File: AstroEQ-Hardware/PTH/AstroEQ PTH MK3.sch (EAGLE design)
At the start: 46 parts, among them IC1 ATMEGA162-16PU, IC2 PIC18F14K50-I/P, IC3 78L05, J1 POWER_JACKPTH, M1 Motor Driver, M2 Motor Driver, X1 16MHz, X2 12MHz

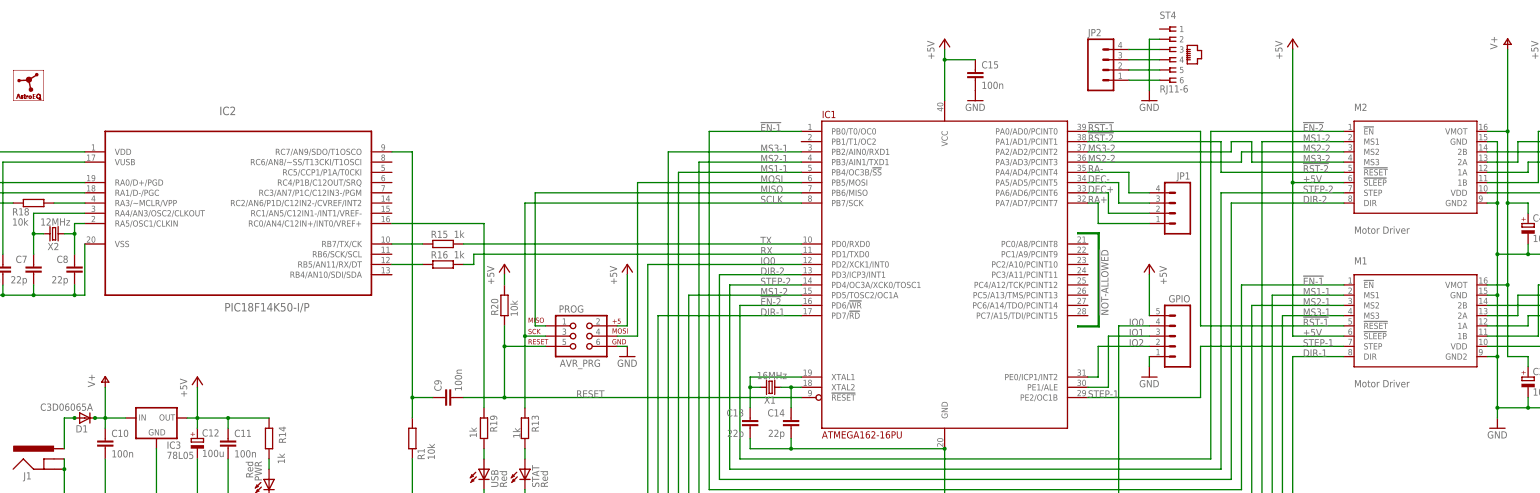
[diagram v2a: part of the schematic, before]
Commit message: Correct Schematic Labelling
Correct labelling in schematic and add additional information to avoid confusion with pin assignments on driver boards.
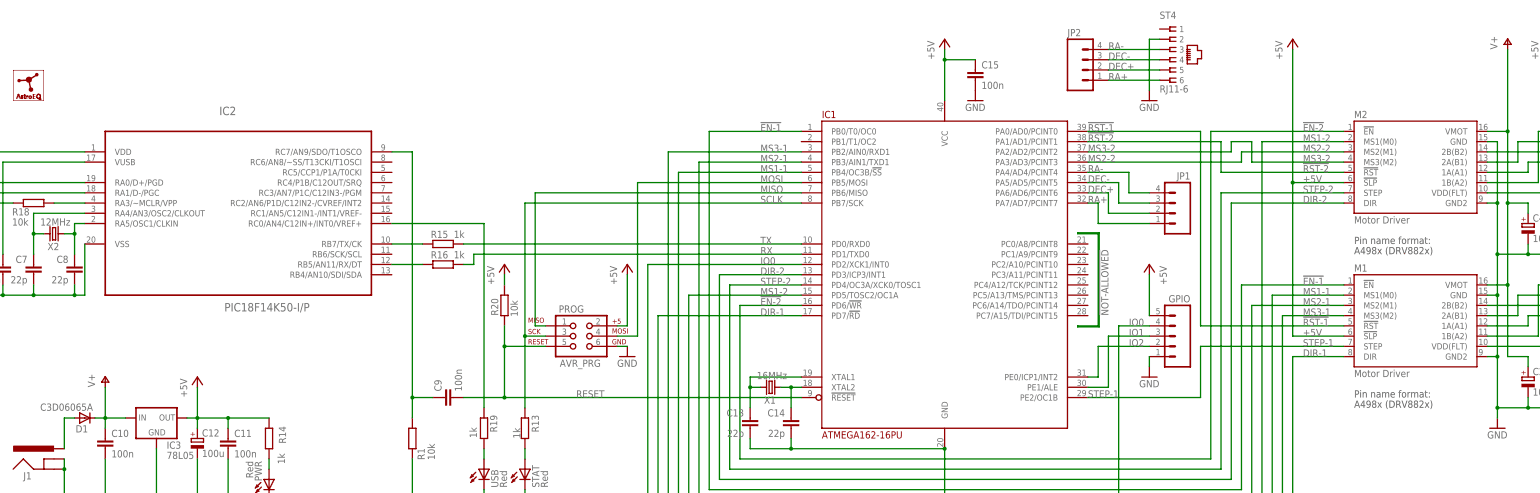
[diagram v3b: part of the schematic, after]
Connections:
- net !RST-1: now also M1.!RST; no longer M1.!RESET
- net !RST-2: now also M2.!RST; no longer M2.!RESET
- net +5V: now also M1.!SLP, M1.VDD(FLT), M2.!SLP, M2.VDD(FLT); no longer M1.!SLEEP, M1.VDD, M2.!SLEEP, M2.VDD
- net DEC-1A: now also M1.1A(A1); no longer M1.1A
- net DEC-1B: now also M1.1B(A2); no longer M1.1B
- net DEC-2A: now also M1.2A(B1); no longer M1.2A
- net DEC-2B: now also M1.2B(B2); no longer M1.2B
- net MS1-1: now also M1.MS1(M0); no longer M1.MS1
- net MS1-2: now also M2.MS1(M0); no longer M2.MS1
- net MS2-1: now also M1.MS2(M1); no longer M1.MS2
- net MS2-2: now also M2.MS2(M1); no longer M2.MS2
- net MS3-1: now also M1.MS3(M2); no longer M1.MS3
- net MS3-2: now also M2.MS3(M2); no longer M2.MS3
- net RA-1A: now also M2.1A(A1); no longer M2.1A
- net RA-1B: now also M2.1B(A2); no longer M2.1B
- net RA-2A: now also M2.2A(B1); no longer M2.2A
- net RA-2B: now also M2.2B(B2); no longer M2.2B
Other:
- moved on the sheet: JP2
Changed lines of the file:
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@@
 <?xml version="1.0" encoding="utf-8"?>
 <!DOCTYPE eagle SYSTEM "eagle.dtd">
-<eagle version="6.6.0">
+<eagle version="6.5.0">
 <drawing>
 <settings>
@@
 <instance part="ST4" gate="G$1" x="317.5" y="266.7"/>
 <instance part="JP1" gate="G$1" x="317.5" y="226.06" rot="MR0"/>
-<instance part="JP2" gate="G$1" x="302.26" y="261.62"/>
+<instance part="JP2" gate="G$1" x="297.18" y="261.62"/>
 <instance part="GPIO" gate="G$1" x="320.04" y="195.58" rot="MR0"/>
 <instance part="P+1" gate="1" x="312.42" y="213.36" rot="MR0"/>
@@
 <junction x="53.34" y="175.26"/>
 <wire x1="50.8" y1="175.26" x2="53.34" y2="175.26" width="0.1524" layer="91"/>
-<junction x="50.8" y="175.26"/>
 <pinref part="D1" gate="1" pin="C"/>
 </segment>
@@
 <pinref part="P+8" gate="1" pin="+5V"/>
 <wire x1="347.98" y1="266.7" x2="347.98" y2="233.68" width="0.1524" layer="91"/>
-<pinref part="M2" gate="G$1" pin="!SLEEP"/>
+<pinref part="M2" gate="G$1" pin="!SLP"/>
 <wire x1="347.98" y1="233.68" x2="360.68" y2="233.68" width="0.1524" layer="91"/>
-<pinref part="M1" gate="G$1" pin="!SLEEP"/>
+<pinref part="M1" gate="G$1" pin="!SLP"/>
 <wire x1="360.68" y1="195.58" x2="347.98" y2="195.58" width="0.1524" layer="91"/>
 <wire x1="347.98" y1="195.58" x2="347.98" y2="233.68" width="0.1524" layer="91"/>
@@
 <segment>
 <pinref part="P+15" gate="1" pin="+5V"/>
-<pinref part="M2" gate="G$1" pin="VDD"/>
+<pinref part="M2" gate="G$1" pin="VDD(FLT)"/>
 <wire x1="411.48" y1="266.7" x2="411.48" y2="231.14" width="0.1524" layer="91"/>
 <wire x1="411.48" y1="231.14" x2="396.24" y2="231.14" width="0.1524" layer="91"/>
-<pinref part="M1" gate="G$1" pin="VDD"/>
+<pinref part="M1" gate="G$1" pin="VDD(FLT)"/>
 <wire x1="411.48" y1="231.14" x2="411.48" y2="193.04" width="0.1524" layer="91"/>
 <wire x1="411.48" y1="193.04" x2="396.24" y2="193.04" width="0.1524" layer="91"/>
@@
 <net name="!RST-1" class="0">
 <segment>
-<pinref part="M1" gate="G$1" pin="!RESET"/>
+<pinref part="M1" gate="G$1" pin="!RST"/>
 <wire x1="360.68" y1="198.12" x2="325.12" y2="198.12" width="0.1524" layer="91"/>
 <wire x1="325.12" y1="198.12" x2="325.12" y2="246.38" width="0.1524" layer="91"/>
@@
 <net name="MS3-2" class="0">
 <segment>
-<pinref part="M2" gate="G$1" pin="MS3"/>
+<pinref part="M2" gate="G$1" pin="MS3(M2)"/>
 <wire x1="360.68" y1="238.76" x2="337.82" y2="238.76" width="0.1524" layer="91"/>
 <wire x1="337.82" y1="238.76" x2="337.82" y2="243.84" width="0.1524" layer="91"/>
@@
 <net name="MS2-2" class="0">
 <segment>
-<pinref part="M2" gate="G$1" pin="MS2"/>
+<pinref part="M2" gate="G$1" pin="MS2(M1)"/>
 <wire x1="360.68" y1="241.3" x2="335.28" y2="241.3" width="0.1524" layer="91"/>
 <wire x1="335.28" y1="241.3" x2="335.28" y2="238.76" width="0.1524" layer="91"/>
@@
 <wire x1="193.04" y1="241.3" x2="193.04" y2="147.32" width="0.1524" layer="91"/>
 <wire x1="345.44" y1="147.32" x2="345.44" y2="200.66" width="0.1524" layer="91"/>
-<pinref part="M1" gate="G$1" pin="MS3"/>
+<pinref part="M1" gate="G$1" pin="MS3(M2)"/>
 <wire x1="345.44" y1="200.66" x2="360.68" y2="200.66" width="0.1524" layer="91"/>
 <label x="350.52" y="200.66" size="1.778" layer="95"/>
@@
 <wire x1="200.66" y1="154.94" x2="337.82" y2="154.94" width="0.1524" layer="91"/>
 <wire x1="200.66" y1="238.76" x2="200.66" y2="154.94" width="0.1524" layer="91"/>
-<pinref part="M1" gate="G$1" pin="MS2"/>
+<pinref part="M1" gate="G$1" pin="MS2(M1)"/>
 <wire x1="337.82" y1="154.94" x2="337.82" y2="203.2" width="0.1524" layer="91"/>
 <wire x1="337.82" y1="203.2" x2="360.68" y2="203.2" width="0.1524" layer="91"/>
@@
 <net name="!RST-2" class="0">
 <segment>
-<pinref part="M2" gate="G$1" pin="!RESET"/>
+<pinref part="M2" gate="G$1" pin="!RST"/>
 <wire x1="360.68" y1="236.22" x2="330.2" y2="236.22" width="0.1524" layer="91"/>
 <wire x1="330.2" y1="236.22" x2="330.2" y2="243.84" width="0.1524" layer="91"/>
@@
 <wire x1="43.18" y1="175.26" x2="43.18" y2="167.64" width="0.1524" layer="91"/>
 <wire x1="43.18" y1="175.26" x2="45.72" y2="175.26" width="0.1524" layer="91"/>
-<junction x="45.72" y="175.26"/>
 <pinref part="D1" gate="1" pin="A"/>
 </segment>
@@
 <net name="DEC-1B" class="0">
 <segment>
-<pinref part="M1" gate="G$1" pin="1B"/>
+<pinref part="M1" gate="G$1" pin="1B(A2)"/>
 <wire x1="396.24" y1="195.58" x2="408.94" y2="195.58" width="0.1524" layer="91"/>
 <wire x1="408.94" y1="195.58" x2="408.94" y2="208.28" width="0.1524" layer="91"/>
@@
 <net name="DEC-1A" class="0">
 <segment>
-<pinref part="M1" gate="G$1" pin="1A"/>
+<pinref part="M1" gate="G$1" pin="1A(A1)"/>
 <wire x1="396.24" y1="198.12" x2="406.4" y2="198.12" width="0.1524" layer="91"/>
 <wire x1="406.4" y1="198.12" x2="406.4" y2="200.66" width="0.1524" layer="91"/>
@@
 <net name="DEC-2B" class="0">
 <segment>
-<pinref part="M1" gate="G$1" pin="2B"/>
+<pinref part="M1" gate="G$1" pin="2B(B2)"/>
 <wire x1="396.24" y1="203.2" x2="426.72" y2="203.2" width="0.1524" layer="91"/>
 <pinref part="DEC" gate="G$1" pin="4"/>
@@
 <net name="DEC-2A" class="0">
 <segment>
-<pinref part="M1" gate="G$1" pin="2A"/>
+<pinref part="M1" gate="G$1" pin="2A(B1)"/>
 <wire x1="396.24" y1="200.66" x2="403.86" y2="200.66" width="0.1524" layer="91"/>
 <wire x1="403.86" y1="200.66" x2="403.86" y2="205.74" width="0.1524" layer="91"/>
@@
 <net name="RA-1B" class="0">
 <segment>
-<pinref part="M2" gate="G$1" pin="1B"/>
+<pinref part="M2" gate="G$1" pin="1B(A2)"/>
 <wire x1="396.24" y1="233.68" x2="408.94" y2="233.68" width="0.1524" layer="91"/>
 <wire x1="408.94" y1="233.68" x2="408.94" y2="246.38" width="0.1524" layer="91"/>
@@
 <net name="RA-1A" class="0">
 <segment>
-<pinref part="M2" gate="G$1" pin="1A"/>
+<pinref part="M2" gate="G$1" pin="1A(A1)"/>
 <wire x1="396.24" y1="236.22" x2="406.4" y2="236.22" width="0.1524" layer="91"/>
 <wire x1="406.4" y1="236.22" x2="406.4" y2="238.76" width="0.1524" layer="91"/>
@@
 <net name="RA-2A" class="0">
 <segment>
-<pinref part="M2" gate="G$1" pin="2A"/>
+<pinref part="M2" gate="G$1" pin="2A(B1)"/>
 <wire x1="396.24" y1="238.76" x2="403.86" y2="238.76" width="0.1524" layer="91"/>
 <wire x1="403.86" y1="238.76" x2="403.86" y2="243.84" width="0.1524" layer="91"/>
@@
 <segment>
 <pinref part="RA" gate="G$1" pin="4"/>
-<pinref part="M2" gate="G$1" pin="2B"/>
+<pinref part="M2" gate="G$1" pin="2B(B2)"/>
 <label x="414.02" y="241.3" size="1.778" layer="95"/>
 <wire x1="426.72" y1="241.3" x2="396.24" y2="241.3" width="0.1524" layer="91"/>
@@
 <wire x1="195.58" y1="149.86" x2="342.9" y2="149.86" width="0.1524" layer="91"/>
 <wire x1="342.9" y1="149.86" x2="342.9" y2="205.74" width="0.1524" layer="91"/>
-<pinref part="M1" gate="G$1" pin="MS1"/>
+<pinref part="M1" gate="G$1" pin="MS1(M0)"/>
 <wire x1="342.9" y1="205.74" x2="360.68" y2="205.74" width="0.1524" layer="91"/>
 <label x="350.52" y="205.74" size="1.778" layer="95"/>
@@
 <net name="MS1-2" class="0">
 <segment>
-<pinref part="M2" gate="G$1" pin="MS1"/>
+<pinref part="M2" gate="G$1" pin="MS1(M0)"/>
 <wire x1="340.36" y1="243.84" x2="360.68" y2="243.84" width="0.1524" layer="91"/>
 <label x="350.52" y="243.84" size="1.778" layer="95"/>
@@
 <pinref part="ST4" gate="G$1" pin="6"/>
 <pinref part="JP2" gate="G$1" pin="1"/>
-<wire x1="307.34" y1="259.08" x2="314.96" y2="259.08" width="0.1524" layer="91"/>
+<wire x1="302.26" y1="259.08" x2="314.96" y2="259.08" width="0.1524" layer="91"/>
+<label x="302.26" y="259.08" size="1.778" layer="95"/>
 </segment>
 </net>
@@
 <pinref part="ST4" gate="G$1" pin="5"/>
 <pinref part="JP2" gate="G$1" pin="2"/>
-<wire x1="307.34" y1="261.62" x2="314.96" y2="261.62" width="0.1524" layer="91"/>
+<wire x1="302.26" y1="261.62" x2="314.96" y2="261.62" width="0.1524" layer="91"/>
+<label x="302.26" y="261.62" size="1.778" layer="95"/>
 </segment>
 </net>
@@
 <pinref part="ST4" gate="G$1" pin="4"/>
 <pinref part="JP2" gate="G$1" pin="3"/>
-<wire x1="307.34" y1="264.16" x2="314.96" y2="264.16" width="0.1524" layer="91"/>
+<wire x1="302.26" y1="264.16" x2="314.96" y2="264.16" width="0.1524" layer="91"/>
+<label x="302.26" y="264.16" size="1.778" layer="95"/>
 </segment>
 </net>
@@
 <pinref part="ST4" gate="G$1" pin="3"/>
 <pinref part="JP2" gate="G$1" pin="4"/>
-<wire x1="307.34" y1="266.7" x2="314.96" y2="266.7" width="0.1524" layer="91"/>
-</segment>
-</net>
+<wire x1="302.26" y1="266.7" x2="314.96" y2="266.7" width="0.1524" layer="91"/>
+<label x="302.26" y="266.7" size="1.778" layer="95"/>
+</segment>
+</net>
